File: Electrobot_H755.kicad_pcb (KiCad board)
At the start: 2 copper layers, 32 parts, among them J1 Conn_XT30M, J10 Conn_01x04, J11 Conn_01x04, J12 Conn_01x04, J13 Conn_01x04, J14 Conn_01x04, J2 Conn_01x04, J3 Conn_01x04, J4 Conn_01x04, J5 Conn_01x04, J6 Conn_01x04, J7 Conn_01x04, J8 Conn_01x04, J9 Conn_01x04, U2 TSR_1-2450

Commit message: Routage de la carte + fichiers gerber
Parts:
- added ?: , , F.Cu at (86.4, 165.1)
- added ?: , , F.Cu at (88.9, 160.0)
- added ?: , , F.Cu at (96.5, 157.5)
- added ?: , , F.Cu at (134.6, 157.5)
- added ?: , , F.Cu at (132.1, 165.1)
- added ?: , , F.Cu at (78.7, 165.1)
- added ?: , , F.Cu at (101.6, 160.0)
- added ?: , , F.Cu at (116.8, 167.6)
- added ?: , , F.Cu at (81.3, 157.5)
- added ?: , , F.Cu at (78.7, 167.6)
- added ?: , , F.Cu at (111.8, 167.6)
- added ?: , , F.Cu at (109.2, 162.6)
- added ?: , , F.Cu at (86.4, 167.6)
- added ?: , , F.Cu at (81.3, 167.6)
- added ?: , , F.Cu at (134.6, 162.6)
- added ?: , , F.Cu at (101.6, 167.6)
- added ?: , , F.Cu at (88.9, 157.5)
- added ?: , , F.Cu at (96.5, 167.6)
- added ?: , , F.Cu at (106.7, 157.5)
- added ?: , , F.Cu at (114.3, 162.6)
- added ?: , , F.Cu at (106.7, 160.0)
- added ?: , , F.Cu at (129.5, 162.6)
- added ?: , , F.Cu at (106.7, 167.6)
- added ?: , , F.Cu at (104.1, 165.1)
- added ?: , , F.Cu at (111.8, 165.1)
- added ?: , , F.Cu at (116.8, 165.1)
- added ?: , , F.Cu at (96.5, 160.0)
- added ?: , , F.Cu at (111.8, 162.6)
- added ?: , , F.Cu at (91.4, 157.5)
- added ?: , , F.Cu at (129.5, 160.0)
- added ?: , , F.Cu at (83.8, 162.6)
- added ?: , , F.Cu at (116.8, 157.5)
- added ?: , , F.Cu at (91.4, 165.1)
- added ?: , , F.Cu at (119.4, 160.0)
- added ?: , , F.Cu at (124.5, 160.0)
- added ?: , , F.Cu at (132.1, 167.6)
- added ?: , , F.Cu at (121.9, 167.6)
- added ?: , , F.Cu at (119.4, 167.6)
- added ?: , , F.Cu at (127.0, 165.1)
- added ?: , , F.Cu at (124.5, 162.6)
- added ?: , , F.Cu at (91.4, 162.6)
- added ?: , , F.Cu at (99.1, 160.0)
- added ?: , , F.Cu at (104.1, 162.6)
- added ?: , , F.Cu at (104.1, 157.5)
- added ?: , , F.Cu at (83.8, 160.0)
- added ?: , , F.Cu at (88.9, 165.1)
- added ?: , , F.Cu at (132.1, 157.5)
- added ?: , , F.Cu at (109.2, 167.6)
- added ?: , , F.Cu at (114.3, 160.0)
- added ?: , , F.Cu at (127.0, 157.5)
- added ?: , , F.Cu at (116.8, 160.0)
- added ?: , , F.Cu at (94.0, 160.0)
- added ?: , , F.Cu at (94.0, 165.1)
- added ?: , , F.Cu at (119.4, 157.5)
- added ?: , , F.Cu at (83.8, 165.1)
- added ?: , , F.Cu at (99.1, 157.5)
- added ?: , , F.Cu at (86.4, 162.6)
- added ?: , , F.Cu at (99.1, 167.6)
- added ?: , , F.Cu at (96.5, 162.6)
- added ?: , , F.Cu at (124.5, 165.1)
- added ?: , , F.Cu at (99.1, 162.6)
- added ?: , , F.Cu at (88.9, 162.6)
- added ?: , , F.Cu at (83.8, 167.6)
- added ?: , , F.Cu at (106.7, 162.6)
- added ?: , , F.Cu at (121.9, 157.5)
- added ?: , , F.Cu at (111.8, 160.0)
- added ?: , , F.Cu at (101.6, 165.1)
- added ?: , , F.Cu at (81.3, 160.0)
- added ?: , , F.Cu at (91.4, 167.6)
- added ?: , , F.Cu at (127.0, 160.0)
- added ?: , , F.Cu at (109.2, 160.0)
- added ?: , , F.Cu at (104.1, 160.0)
- added ?: , , F.Cu at (121.9, 160.0)
- added ?: , , F.Cu at (83.8, 157.5)
- added ?: , , F.Cu at (114.3, 157.5)
- added ?: , , F.Cu at (116.8, 162.6)
- added ?: , , F.Cu at (81.3, 165.1)
- added ?: , , F.Cu at (101.6, 162.6)
- added ?: , , F.Cu at (134.6, 167.6)
- added ?: , , F.Cu at (94.0, 157.5)
- added ?: , , F.Cu at (124.5, 157.5)
- added ?: , , F.Cu at (78.7, 160.0)
- added ?: , , F.Cu at (99.1, 165.1)
- added ?: , , F.Cu at (132.1, 162.6)
- added ?: , , F.Cu at (114.3, 165.1)
- added ?: , , F.Cu at (124.5, 167.6)
- added ?: , , F.Cu at (101.6, 157.5)
- added ?: , , F.Cu at (134.6, 160.0)
- added ?: , , F.Cu at (78.7, 157.5)
- added ?: , , F.Cu at (86.4, 160.0)
- added ?: , , F.Cu at (109.2, 157.5)
- added ?: , , F.Cu at (81.3, 162.6)
- added ?: , , F.Cu at (129.5, 165.1)
- added ?: , , F.Cu at (94.0, 167.6)
- added ?: , , F.Cu at (78.7, 162.6)
- added ?: , , F.Cu at (111.8, 157.5)
- added ?: , , F.Cu at (121.9, 162.6)
- added ?: , , F.Cu at (114.3, 167.6)
- added ?: , , F.Cu at (106.7, 165.1)
- added ?: , , F.Cu at (129.5, 167.6)
- added ?: , , F.Cu at (109.2, 165.1)
- added ?: , , F.Cu at (86.4, 157.5)
- added ?: , , F.Cu at (88.9, 167.6)
- added ?: , , F.Cu at (94.0, 162.6)
- added ?: , , F.Cu at (132.1, 160.0)
- added ?: , , F.Cu at (91.4, 160.0)
- added ?: , , F.Cu at (134.6, 165.1)
- added ?: , , F.Cu at (119.4, 165.1)
- added ?: , , F.Cu at (119.4, 162.6)
- added ?: , , F.Cu at (127.0, 162.6)
- added ?: , , F.Cu at (121.9, 165.1)
- added ?: , , F.Cu at (129.5, 157.5)
- added ?: , , F.Cu at (104.1, 167.6)
- added ?: , , F.Cu at (96.5, 165.1)
- added ?: , , F.Cu at (127.0, 167.6)
- added C10: 220u, Passive:C_Radial_D8.0mm_H11.5mm_P3.50mm, B.Cu at (91.9, 63.8)
- added C11: 220u, Passive:C_Radial_D8.0mm_H11.5mm_P3.50mm, B.Cu at (114.5, 53.0)
- added C12: 220u, Passive:C_Radial_D8.0mm_H11.5mm_P3.50mm, B.Cu at (114.5, 41.7)
- added C13: Value, Capacitor_SMD:C_1206_3216Metric, F.Cu at (102.4, 72.1)
- added C14: 100n, Capacitor_SMD:C_1206_3216Metric, F.Cu at (114.6, 122.2)
- added C15: 100n, Capacitor_SMD:C_1206_3216Metric, F.Cu at (148.1, 130.6)
- added C16: 100n, Capacitor_SMD:C_1206_3216Metric, F.Cu at (81.3, 74.9)
- added C17: Value, Capacitor_SMD:C_1206_3216Metric, B.Cu at (136.1, 90.2)
- added C18: 100n, Capacitor_SMD:C_1206_3216Metric, F.Cu at (114.8, 95.5)
- added C19: 100n, Capacitor_SMD:C_1206_3216Metric, F.Cu at (93.7, 85.1)
- added C20: 100n, Capacitor_SMD:C_1206_3216Metric, F.Cu at (96.3, 101.9)
- added C3: Value, Capacitor_SMD:C_1206_3216Metric, F.Cu at (122.2, 132.8)
- added C6: Value, Capacitor_SMD:C_1206_3216Metric, F.Cu at (74.7, 106.7)
- added C7: Value, Capacitor_SMD:C_1206_3216Metric, F.Cu at (69.3, 121.9)
- added C8: Value, Capacitor_SMD:C_1206_3216Metric, F.Cu at (135.9, 84.1)
- added C9: 47u, Capacitor_SMD:C_1206_3216Metric, F.Cu at (119.1, 142.0)
- added D4: LED, LED_SMD:LED_1206_3216Metric, B.Cu at (107.0, 147.8)
- added J15: Conn_01x03, Connector_Molex:Molex_KK-254_AE-6410-03A_1x03_P2.54mm_Vertical, B.Cu at (122.8, 138.7)
- added J16: Conn_01x03, Connector_Molex:Molex_KK-254_AE-6410-03A_1x03_P2.54mm_Vertical, B.Cu at (68.0, 103.6)
- added J17: Conn_01x04, Connector_Molex:Molex_KK-254_AE-6410-04A_1x04_P2.54mm_Vertical, B.Cu at (139.2, 85.2)
- added J18: Conn_01x03, Servomotors:Servomotor-3x254, B.Cu at (129.3, 60.2)
- added J19: Conn_01x03, Servomotors:Servomotor-3x254, B.Cu at (129.3, 50.3)
- added J20: Conn_01x03, Servomotors:Servomotor-3x254, B.Cu at (129.3, 56.9)
- added J21: Conn_01x03, Servomotors:Servomotor-3x254, B.Cu at (129.3, 47.0)
- added J22: Conn_01x04, Connector_Molex:Molex_KK-254_AE-6410-04A_1x04_P2.54mm_Vertical, B.Cu at (145.1, 98.5)
- added J23: Conn_01x03, Servomotors:Servomotor-3x254, B.Cu at (129.3, 43.7)
- added J24: Conn_01x03, Servomotors:Servomotor-3x254, B.Cu at (129.3, 40.3)
- added J25: Conn_01x03, Servomotors:Servomotor-3x254, B.Cu at (129.3, 53.6)
- added J26: Conn_01x03, Connector_Molex:Molex_KK-254_AE-6410-03A_1x03_P2.54mm_Vertical, B.Cu at (68.0, 115.7)
- added J27: Conn_01x02, Connector_Molex:Molex_KK-254_AE-6410-02A_1x02_P2.54mm_Vertical, B.Cu at (77.8, 118.2)
- added J28: Conn_01x02, Connector_Molex:Molex_KK-254_AE-6410-02A_1x02_P2.54mm_Vertical, B.Cu at (77.8, 110.0)
- added J29: Conn_01x02, Connector_Molex:Molex_KK-254_AE-6410-02A_1x02_P2.54mm_Vertical, B.Cu at (139.4, 66.7)
- added J30: Conn_01x02, Connector_Molex:Molex_KK-254_AE-6410-02A_1x02_P2.54mm_Vertical, B.Cu at (139.4, 75.0)
- added J31: Conn_01x03, Connector_Molex:Molex_KK-254_AE-6410-03A_1x03_P2.54mm_Vertical, B.Cu at (92.4, 99.1)
- added J32: Conn_01x03, Connector_Molex:Molex_KK-254_AE-6410-03A_1x03_P2.54mm_Vertical, B.Cu at (77.1, 95.8)
- added J33: Conn_01x06, Connector_Molex:Molex_KK-254_AE-6410-06A_1x06_P2.54mm_Vertical, B.Cu at (92.4, 79.5)
- added J34: Conn_01x06, Connector_Molex:Molex_KK-254_AE-6410-06A_1x06_P2.54mm_Vertical, B.Cu at (92.4, 90.3)
- added J35: Conn_01x04, Connector_Molex:Molex_KK-254_AE-6410-04A_1x04_P2.54mm_Vertical, B.Cu at (139.9, 134.1)
- added J36: Conn_01x02, Connector_Molex:Molex_KK-254_AE-6410-02A_1x02_P2.54mm_Vertical, B.Cu at (77.1, 87.1)
- added J37: Conn_01x04, Connector_Molex:Molex_KK-254_AE-6410-04A_1x04_P2.54mm_Vertical, B.Cu at (139.7, 109.2)
- added JP1: SolderJumper_2_Open, Connector_PinHeader_2.54mm:PinHeader_1x02_P2.54mm_Vertical, B.Cu at (122.8, 47.9)
- added R1: 10k, Resistor_SMD:R_1206_3216Metric, F.Cu at (120.1, 103.8)
- added R10: 10k, Resistor_SMD:R_1206_3216Metric, F.Cu at (122.7, 121.9)
- added R11: 10k, Resistor_SMD:R_1206_3216Metric, F.Cu at (122.4, 77.0)
- added R12: 10k, Resistor_SMD:R_1206_3216Metric, F.Cu at (125.0, 69.3)
- added R13: 18k, Resistor_SMD:R_1206_3216Metric, F.Cu at (122.7, 119.1)
- added R14: 18k, Resistor_SMD:R_1206_3216Metric, F.Cu at (124.5, 126.0)
- added R15: 18k, Resistor_SMD:R_1206_3216Metric, F.Cu at (125.2, 82.0)
- added R16: 18k, Resistor_SMD:R_1206_3216Metric, F.Cu at (125.0, 66.3)
- added R2: 18k, Resistor_SMD:R_1206_3216Metric, F.Cu at (135.9, 101.6)
- added R22: R, Resistor_SMD:R_1206_3216Metric, B.Cu at (126.2, 137.2)
- added R23: R, Resistor_SMD:R_1206_3216Metric, F.Cu at (122.2, 135.4)
- added R24: R, Resistor_SMD:R_1206_3216Metric, B.Cu at (69.3, 106.7)
- added R25: R, Resistor_SMD:R_1206_3216Metric, F.Cu at (70.9, 102.6)
- added R26: R, Resistor_SMD:R_1206_3216Metric, B.Cu at (69.3, 118.6)
- added R27: R, Resistor_SMD:R_1206_3216Metric, F.Cu at (72.4, 115.6)
- added R28: R, Resistor_SMD:R_1206_3216Metric, B.Cu at (136.9, 80.2)
- added R29: R, Resistor_SMD:R_1206_3216Metric, B.Cu at (135.4, 84.1)
- added R3: 10k, Resistor_SMD:R_1206_3216Metric, F.Cu at (120.4, 97.5)
- added R30: 39k, Resistor_SMD:R_1206_3216Metric, F.Cu at (102.4, 69.1)
- added R31: 10k, Resistor_SMD:R_1206_3216Metric, F.Cu at (80.0, 104.6)
- added R32: 10k, Resistor_SMD:R_1206_3216Metric, F.Cu at (92.7, 110.5)
- added R33: 18k, Resistor_SMD:R_1206_3216Metric, F.Cu at (89.9, 113.3)
- added R34: 10k, Resistor_SMD:R_1206_3216Metric, F.Cu at (136.1, 95.2)
- added R35: 18k, Resistor_SMD:R_1206_3216Metric, F.Cu at (136.1, 92.2)
- added R36: 470, Resistor_SMD:R_1206_3216Metric, F.Cu at (106.9, 149.1)
- added R37: R, Resistor_SMD:R_1206_3216Metric, B.Cu at (142.0, 89.9)
- added R38: R, Resistor_SMD:R_1206_3216Metric, F.Cu at (136.1, 89.7)
- added R4: 18k, Resistor_SMD:R_1206_3216Metric, F.Cu at (79.8, 121.7)
- added R5: 10k, Resistor_SMD:R_1206_3216Metric, F.Cu at (120.1, 88.3)
- added R6: 10k, Resistor_SMD:R_1206_3216Metric, F.Cu at (125.2, 91.9)
- added R7: 18k, Resistor_SMD:R_1206_3216Metric, F.Cu at (125.2, 84.8)
- added R8: 18k, Resistor_SMD:R_1206_3216Metric, F.Cu at (125.2, 94.7)
- added R9: 10k, Resistor_SMD:R_1206_3216Metric, F.Cu at (119.9, 129.5)
- added U3: TSR_2-2465, Converter_DCDC:Converter_DCDC_TRACO_TSR-1_THT, B.Cu at (99.2, 52.5)
- added U4: TSR_2-2465, Converter_DCDC:Converter_DCDC_TRACO_TSR-1_THT, B.Cu at (99.2, 41.7)
- C4: footprint Capacitor_THT:C_Radial_D8.0mm_H11.5mm_P3.50mm -> Passive:C_Radial_D8.0mm_H11.5mm_P3.50mm; moved to B.Cu
- D1, D2, D3, J1: moved to B.Cu
- U2: value TSR_1-2450 -> TSR_2-2450; moved to B.Cu
- moved H3 170.4 mm to (147.3, 40.7)
- moved H4 117.0 mm to (147.3, 166.4)
- moved H1 114.5 mm to (68.2, 40.7)
- moved U2 107.3 mm to (88.4, 56.1), turned to 180 degrees
- moved C1 100.2 mm to (84.8, 52.8)
- moved J5 96.9 mm to (77.1, 134.7), turned to 90 degrees
- moved J2 93.5 mm to (92.3, 126.2), turned to 90 degrees
- moved J3 92.6 mm to (92.4, 132.8), turned to -90 degrees
- moved C2 89.9 mm to (74.2, 97.0), turned to -90 degrees
- moved J6 88.3 mm to (97.5, 108.0), turned to -90 degrees
- moved J1 75.0 mm to (84.0, 42.2)
- moved J9 71.4 mm to (113.5, 125.5), turned to 0 degrees
- moved R17 68.1 mm to (141.6, 157.3), turned to 90 degrees
- moved J7 66.8 mm to (113.5, 100.7), turned to 0 degrees
- moved R18 64.1 mm to (144.7, 157.3), turned to 90 degrees
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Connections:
- J6 pad 1: /RS232_1_TX -> /RS232_2_TX
- J6 pad 2: /RS232_1_RX -> Net-(J6-Pin_2)
- J6 pad 3: /RS232_1_GPIO -> /RS232_2_DIR
- R19 pad 1: /LED1 -> /LED4
- R20 pad 1: /LED2 -> /LED5
- R21 pad 1: /LED3 -> /LED6
- U1 pad CN10_10: unconnected-(U1-PE13-PadCN10_10) -> /Mot3_Sens2
- U1 pad CN10_12: unconnected-(U1-PG14-PadCN10_12) -> /RS232_3_TX
- U1 pad CN10_14: unconnected-(U1-PB6-PadCN10_14) -> /I2C_SCL
- U1 pad CN10_15: unconnected-(U1-PB2-PadCN10_15) -> /SPI_MOSI
- U1 pad CN10_16: unconnected-(U1-PB7-PadCN10_16) -> /I2C_SDA
- U1 pad CN10_17: unconnected-(U1-GND-PadCN10_17) -> GND
- U1 pad CN10_18: unconnected-(U1-PE8-PadCN10_18) -> /LED5
- U1 pad CN10_19: unconnected-(U1-PD13-PadCN10_19) -> /CODER_3_B
- U1 pad CN10_20: unconnected-(U1-PE7-PadCN10_20) -> /LED4
- U1 pad CN10_21: unconnected-(U1-PD12-PadCN10_21) -> /CODER_3_A
- U1 pad CN10_22: unconnected-(U1-GND-PadCN10_22) -> GND
- U1 pad CN10_23: unconnected-(U1-PD11-PadCN10_23) -> /Mot2_Sens2
- U1 pad CN10_26: unconnected-(U1-PE12-PadCN10_26) -> /LED6
- U1 pad CN10_27: unconnected-(U1-GND-PadCN10_27) -> GND
- U1 pad CN10_29: unconnected-(U1-PA0-PadCN10_29) -> /Eana1f
- U1 pad CN10_3: unconnected-(U1-AGND-PadCN10_3) -> GND
- U1 pad CN10_30: unconnected-(U1-PE15-PadCN10_30) -> /LED7
- U1 pad CN10_32: unconnected-(U1-PB10-PadCN10_32) -> /Servo5_PWM
- U1 pad CN10_34: unconnected-(U1-PB11-PadCN10_34) -> /Servo4_PWM
- U1 pad CN10_5: unconnected-(U1-GND-PadCN10_5) -> GND
- U1 pad CN10_6: unconnected-(U1-PE11-PadCN10_6) -> /CODER_1_B
- U1 pad CN10_7: unconnected-(U1-PF6-PadCN10_7) -> /Mot3_PWM
- U1 pad CN10_8: unconnected-(U1-PE14-PadCN10_8) -> /Mot3_Sens1
- U1 pad CN7_1: unconnected-(U1-PC6-PadCN7_1) -> /CODER_4_A
- U1 pad CN7_10: unconnected-(U1-PA5-PadCN7_10) -> /Servo3_PWM
- U1 pad CN7_11: unconnected-(U1-PC7-PadCN7_11) -> /CODER_4_B
- U1 pad CN7_12: unconnected-(U1-PA6-PadCN7_12) -> /Eana4f
- U1 pad CN7_13: unconnected-(U1-PB5-PadCN7_13) -> /CODER_2_B
- U1 pad CN7_15: unconnected-(U1-PB3-PadCN7_15) -> /Servo2_PWM
- U1 pad CN7_17: unconnected-(U1-PA4-PadCN7_17) -> /Eana5f
- U1 pad CN7_19: unconnected-(U1-PB4-PadCN7_19) -> /CODER_2_A
- U1 pad CN7_2: unconnected-(U1-PB8-PadCN7_2) -> /Etor3
- U1 pad CN7_20: unconnected-(U1-PG9-PadCN7_20) -> /RS232_3_RX
- U1 pad CN7_3: unconnected-(U1-PB15-PadCN7_3) -> /Servo1_PWM
- U1 pad CN7_4: unconnected-(U1-PB9-PadCN7_4) -> /Etor4
- U1 pad CN7_8: unconnected-(U1-GND-PadCN7_8) -> GND
- U1 pad CN8_10: unconnected-(U1-PC12-PadCN8_10) -> /LED_RGB
- U1 pad CN8_2: unconnected-(U1-PC8-PadCN8_2) -> /SPI_CS1
- U1 pad CN8_4: unconnected-(U1-PC9-PadCN8_4) -> /SPI_CS2
- U1 pad CN8_5: unconnected-(U1-~{RESET}-PadCN8_5) -> Net-(J36-Pin_1)
- U1 pad CN8_6: unconnected-(U1-PC10-PadCN8_6) -> /SPI_CLK
- U1 pad CN8_8: unconnected-(U1-PC11-PadCN8_8) -> /SPI_MISO
- U1 pad CN9_1: unconnected-(U1-PA3-PadCN9_1) -> /Eana2f
- U1 pad CN9_12: unconnected-(U1-GND-PadCN9_12) -> GND
- U1 pad CN9_14: unconnected-(U1-PE2-PadCN9_14) -> /Mot1_Sens1
- U1 pad CN9_15: unconnected-(U1-PE9-PadCN9_15) -> /CODER_1_A
- U1 pad CN9_16: unconnected-(U1-PE4-PadCN9_16) -> /Mot1_Sens2
- U1 pad CN9_18: unconnected-(U1-PE5-PadCN9_18) -> /Mot1_PWM
- U1 pad CN9_19: unconnected-(U1-PF14-PadCN9_19) -> /Mot4_Sens1
- U1 pad CN9_20: unconnected-(U1-PE6-PadCN9_20) -> /Mot2_PWM
- U1 pad CN9_21: unconnected-(U1-PF15-PadCN9_21) -> /Mot4_Sens2
- U1 pad CN9_22: unconnected-(U1-PE3-PadCN9_22) -> /Mot2_Sens1
- U1 pad CN9_23: unconnected-(U1-GND-PadCN9_23) -> GND
- U1 pad CN9_24: unconnected-(U1-PF8-PadCN9_24) -> /Servo6_PWM
- U1 pad CN9_26: unconnected-(U1-PF7-PadCN9_26) -> /Mot4_PWM
- U1 pad CN9_28: unconnected-(U1-PF9-PadCN9_28) -> /Servo7_PWM
- U1 pad CN9_3: unconnected-(U1-PC0-PadCN9_3) -> /VBATf
- U1 pad CN9_4: unconnected-(U1-PD6-PadCN9_4) -> /RS232_2_RX
- U1 pad CN9_5: unconnected-(U1-PC3-PadCN9_5) -> /Etor2
- U1 pad CN9_6: unconnected-(U1-PD5-PadCN9_6) -> /RS232_2_TX
- U1 pad CN9_7: unconnected-(U1-PB1-PadCN9_7) -> /Eana3f
- U1 pad CN9_8: unconnected-(U1-PD4-PadCN9_8) -> /RS232_2_DIR
- U1 pad CN9_9: unconnected-(U1-PC2-PadCN9_9) -> /Etor1
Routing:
- net +5V: track 0.00 -> 494.7 mm, vias 0 -> 1
- net GND: track 0.00 -> 281.7 mm, vias 0 -> 1
- net /Servo7_PWM: track 0.00 -> 161.3 mm
- net +3.3V: track 0.00 -> 159.1 mm, vias 0 -> 1
- net /Servo5_PWM: track 0.00 -> 124.5 mm
- net /Servo6_PWM: track 0.00 -> 116.9 mm
- net /I2C_SCL: track 0.00 -> 101.4 mm
- net /Servo4_PWM: track 0.00 -> 100.6 mm
- net /I2C_SDA: track 0.00 -> 83.3 mm
- net /SPI_MOSI: track 0.00 -> 60.5 mm, vias 0 -> 1
- net /CODER_1_A: track 0.00 -> 58.9 mm, vias 0 -> 1
- net /VBATf: track 0.00 -> 58.0 mm, vias 0 -> 1
- net /LED5: track 0.00 -> 56.0 mm
- net /VBAT: track 0.00 -> 54.3 mm
- net /+Vservo1: track 0.00 -> 51.0 mm
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- added copper zone on B.Cu, net GND
- added copper zone on F.Cu, net GND
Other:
- board outline added: 88.3 x 136 mm
- board text added: "+"
- board text added: "+3.3V"
- board text added: "+5V"
- board text added: "-"
- board text added: "1"
- board text added: "2"
- board text added: "3"
- board text added: "4"
- board text added: "5"
- board text added: "6"
- board text added: "7"
- board text added: "CS1"
- board text added: "CS2"
- board text added: "Codeur1"
- board text added: "Codeur2"
- board text added: "Codeur3"
- board text added: "Codeur4"
- board text added: "Dir"
- board text added: "ELECTROBOT_H755 V1 (2025)"
- board text added: "Eana"
- board text added: "Etor"
- board text added: "GND"
- board text added: "I2C"
- board text added: "I2C_SCL"
- board text added: "I2C_SDA"
- board text added: "MISO"
- board text added: "MOSI"
- board text added: "Moteur1"
- board text added: "Moteur2"
- board text added: "Moteur3"
- board text added: "Moteur4"
- board text added: "PROTOTYPAGE"
- board text added: "RS232"
- board text added: "RS232 AX"
- board text added: "RX"
- board text added: "Reset"
- board text added: "SCK"
- board text added: "SCL"
- board text added: "SDA"
- board text added: "SPI"
- board text added: "Servo"
- board text added: "TX"

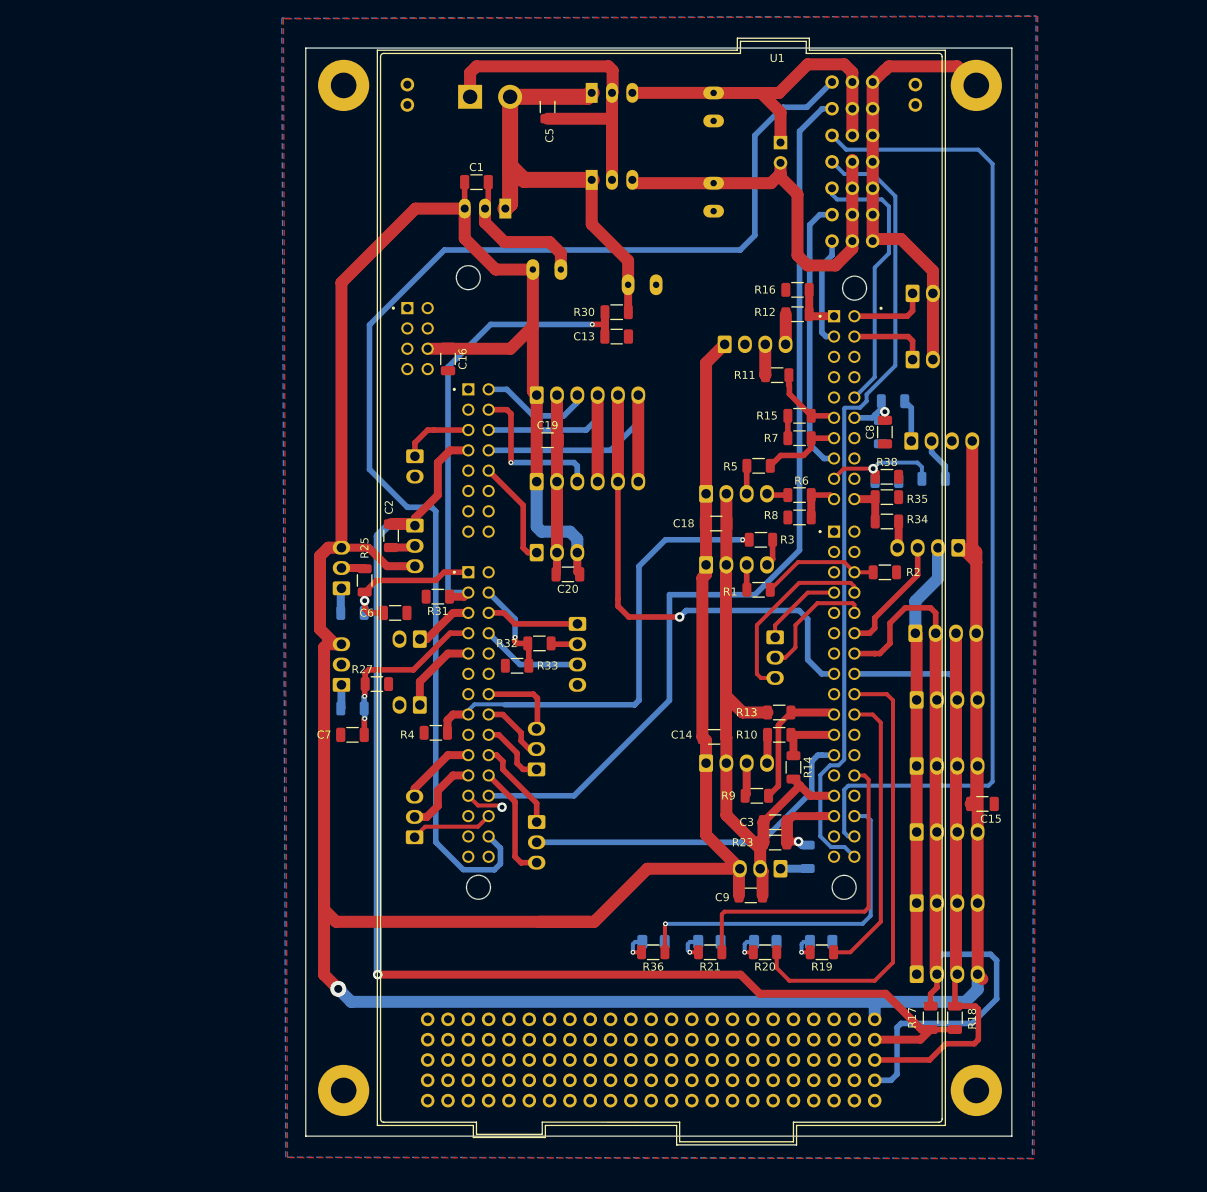
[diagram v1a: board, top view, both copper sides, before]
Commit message: Bords de la carte arrondis + ajout sérigraphie manquante
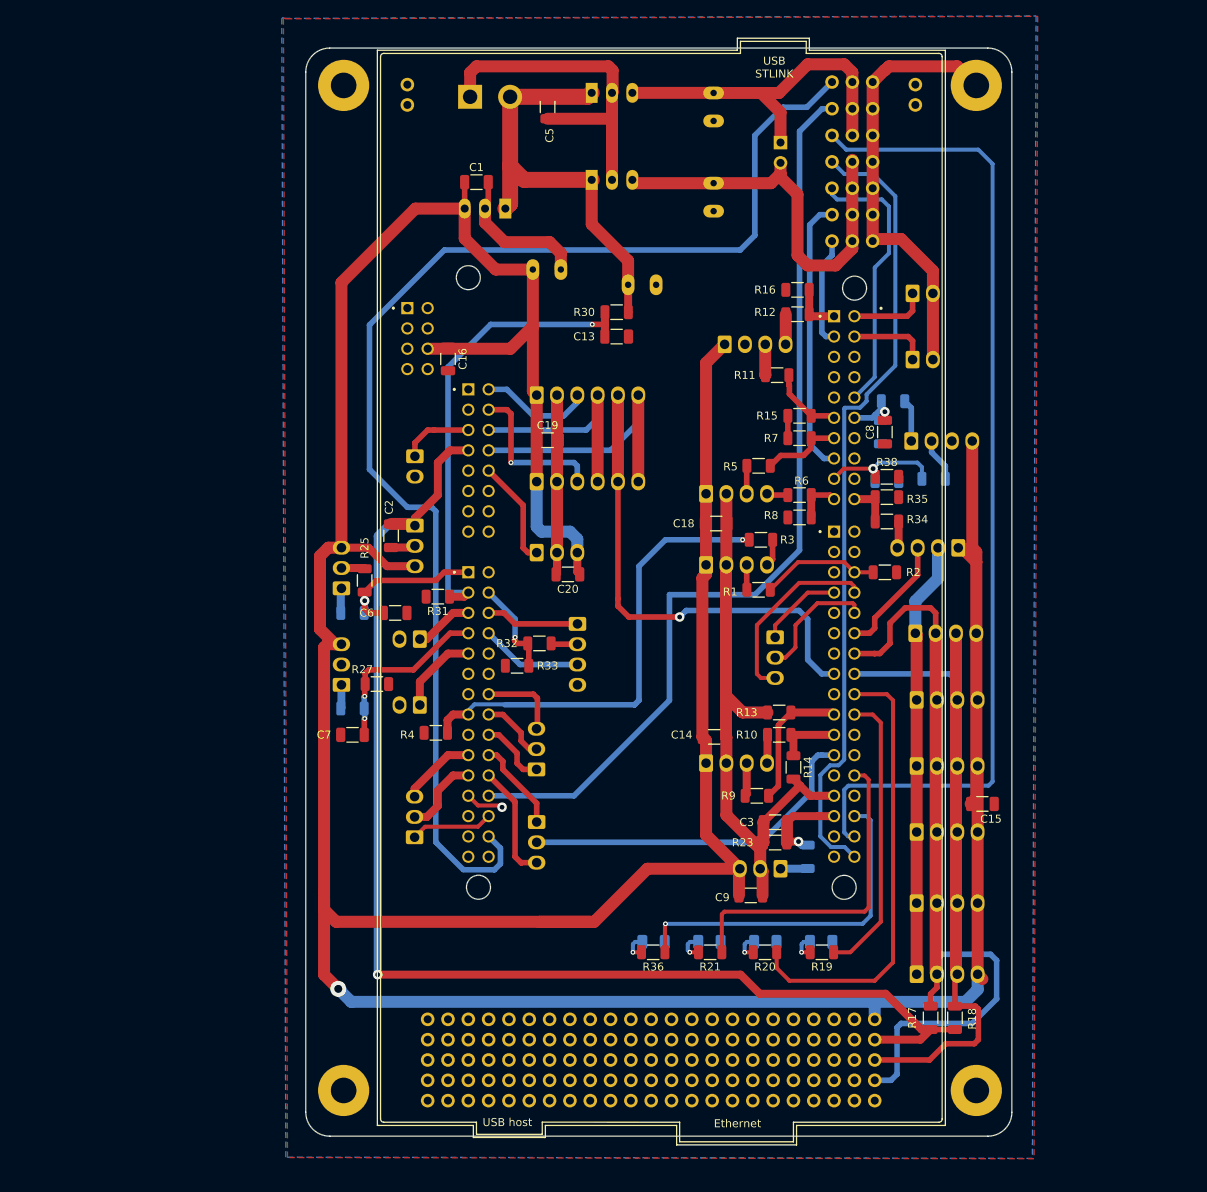
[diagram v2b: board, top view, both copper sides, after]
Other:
- outline, holes or cut-outs redrawn
- board text added: "Ethernet"
- board text added: "USB STLINK"
- board text added: "USB host"
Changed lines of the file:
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@@
 			(at 46.228 -31.242 0)
 			(layer "F.SilkS")
+			(hide yes)
 			(effects
 				(font
@@
 		(layer "B.SilkS")
 	)
-	(gr_rect
-		(start 63.5 36.068)
-		(end 151.765 172.085)
+	(gr_arc
+		(start 66.5 172.085)
+		(mid 64.37868 171.20632)
+		(end 63.5 169.085)
+		(locked yes)
+		(stroke
+			(width 0.05)
+			(type default)
+		)
+		(layer "Edge.Cuts")
+	)
+	(gr_line
+		(start 148.765 172.085)
+		(end 66.5 172.085)
+		(locked yes)
+		(stroke
+			(width 0.05)
+			(type default)
+		)
+		(layer "Edge.Cuts")
+	)
+	(gr_line
+		(start 66.5 36.068)
+		(end 148.765 36.068)
+		(locked yes)
+		(stroke
+			(width 0.05)
+			(type default)
+		)
+		(layer "Edge.Cuts")
+	)
+	(gr_line
+		(start 151.765 39.068)
+		(end 151.765 169.085)
+		(locked yes)
+		(stroke
+			(width 0.05)
+			(type default)
+		)
+		(layer "Edge.Cuts")
+	)
+	(gr_arc
+		(start 148.765 36.068)
+		(mid 150.88632 36.94668)
+		(end 151.765 39.068)
+		(locked yes)
+		(stroke
+			(width 0.05)
+			(type default)
+		)
+		(layer "Edge.Cuts")
+	)
+	(gr_arc
+		(start 151.765 169.085)
+		(mid 150.88632 171.20632)
+		(end 148.765 172.085)
+		(locked yes)
+		(stroke
+			(width 0.05)
+			(type default)
+		)
+		(layer "Edge.Cuts")
+	)
+	(gr_line
+		(start 63.5 169.085)
+		(end 63.5 39.068)
+		(locked yes)
+		(stroke
+			(width 0.05)
+			(type default)
+		)
+		(layer "Edge.Cuts")
+	)
+	(gr_arc
+		(start 63.5 39.068)
+		(mid 64.37868 36.94668)
+		(end 66.5 36.068)
 		(locked yes)
 		(stroke
@@
 			(type default)
 		)
-		(fill none)
 		(layer "Edge.Cuts")
 	)
@@
 		)
 	)
+	(gr_text "USB host"
+		(at 85.598 170.942 -0)
+		(layer "F.SilkS")
+		(effects
+			(font
+				(size 1 1)
+				(thickness 0.1)
+			)
+			(justify left bottom)
+		)
+	)
+	(gr_text "Ethernet"
+		(at 114.5032 171.0944 -0)
+		(layer "F.SilkS")
+		(effects
+			(font
+				(size 1 1)
+				(thickness 0.1)
+			)
+			(justify left bottom)
+		)
+	)
+	(gr_text "USB\nSTLINK"
+		(at 122.0724 39.878 0)
+		(layer "F.SilkS")
+		(effects
+			(font
+				(size 1 1)
+				(thickness 0.1)
+			)
+			(justify bottom)
+		)
+	)

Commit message: Ajout sérigraphie manquante
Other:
- board text added: "A"
- board text added: "K"
- board text added: "PWM"
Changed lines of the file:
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@@
+		)
+	)
+	(gr_text "A"
+		(at 126.8984 150.368 0)
+		(layer "B.SilkS")
+		(effects
+			(font
+				(size 1 1)
+				(thickness 0.1)
+			)
+			(justify left bottom mirror)
 		)
 	)
@@
 		)
 	)
+	(gr_text "A"
+		(at 113.0808 150.3172 0)
+		(layer "B.SilkS")
+		(effects
+			(font
+				(size 1 1)
+				(thickness 0.1)
+			)
+			(justify left bottom mirror)
+		)
+	)
+	(gr_text "+"
+		(at 132.2832 62.0268 90)
+		(layer "B.SilkS")
+		(effects
+			(font
+				(size 1 1)
+				(thickness 0.1)
+			)
+			(justify left bottom mirror)
+		)
+	)
 	(gr_text "1"
 		(at 127.5588 60.8584 0)
@@
 		)
 	)
+	(gr_text "A"
+		(at 119.9896 150.368 0)
+		(layer "B.SilkS")
+		(effects
+			(font
+				(size 1 1)
+				(thickness 0.1)
+			)
+			(justify left bottom mirror)
+		)
+	)
 	(gr_text "-"
 		(at 143.002 93.472 90)
@@
 		)
 	)
+	(gr_text "-"
+		(at 95.9612 60.9092 90)
+		(layer "B.SilkS")
+		(effects
+			(font
+				(size 1 1)
+				(thickness 0.1)
+			)
+			(justify left bottom mirror)
+		)
+	)
+	(gr_text "-"
+		(at 116.1796 44.6532 180)
+		(layer "B.SilkS")
+		(effects
+			(font
+				(size 1 1)
+				(thickness 0.1)
+			)
+			(justify left bottom mirror)
+		)
+	)
 	(gr_text "+5V"
 		(at 136.398 156.4132 0)
@@
 		)
 	)
+	(gr_text "K"
+		(at 116.078 150.368 0)
+		(layer "B.SilkS")
+		(effects
+			(font
+				(size 1 1)
+				(thickness 0.1)
+			)
+			(justify left bottom mirror)
+		)
+	)
 	(gr_text "5"
 		(at 127.5588 47.6504 0)
@@
 		)
 	)
+	(gr_text "-"
+		(at 134.9248 62.1792 90)
+		(layer "B.SilkS")
+		(effects
+			(font
+				(size 1 1)
+				(thickness 0.1)
+			)
+			(justify left bottom mirror)
+		)
+	)
 	(gr_text "+"
 		(at 114.1984 87.1728 90)
@@
 		)
 	)
+	(gr_text "+"
+		(at 117.1448 40.9448 90)
+		(layer "B.SilkS")
+		(effects
+			(font
+				(size 1 1)
+				(thickness 0.1)
+			)
+			(justify left bottom mirror)
+		)
+	)
 	(gr_text "-"
 		(at 95.5548 84.4804 90)
@@
 		)
 	)
+	(gr_text "PWM"
+		(at 129.6924 62.23 90)
+		(layer "B.SilkS")
+		(effects
+			(font
+				(size 1 1)
+				(thickness 0.1)
+				(italic yes)
+			)
+			(justify left bottom mirror)
+		)
+	)
+	(gr_text "K"
+		(at 129.8448 150.4188 0)
+		(layer "B.SilkS")
+		(effects
+			(font
+				(size 1 1)
+				(thickness 0.1)
+			)
+			(justify left bottom mirror)
+		)
+	)
 	(gr_text "-"
 		(at 101.346 115.316 180)
@@
 		)
 	)
+	(gr_text "+"
+		(at 104.2924 62.4332 90)
+		(layer "B.SilkS")
+		(effects
+			(font
+				(size 1 1)
+				(thickness 0.1)
+			)
+			(justify left bottom mirror)
+		)
+	)
 	(gr_text "Codeur2"
 		(at 111.2012 88.5444 90)
@@
 	)
 	(gr_text "-"
+		(at 107.8992 62.3824 90)
+		(layer "B.SilkS")
+		(effects
+			(font
+				(size 1 1)
+				(thickness 0.1)
+			)
+			(justify left bottom mirror)
+		)
+	)
+	(gr_text "K"
+		(at 108.9152 150.4696 0)
+		(layer "B.SilkS")
+		(effects
+			(font
+				(size 1 1)
+				(thickness 0.1)
+			)
+			(justify left bottom mirror)
+		)
+	)
+	(gr_text "-"
 		(at 116.6368 104.2924 90)
 		(layer "B.SilkS")
@@
 		)
 	)
+	(gr_text "K"
+		(at 122.8852 150.4188 0)
+		(layer "B.SilkS")
+		(effects
+			(font
+				(size 1 1)
+				(thickness 0.1)
+			)
+			(justify left bottom mirror)
+		)
+	)
 	(gr_text "+"
 		(at 116.5352 68.4784 90)
@@
 	)
 	(gr_text "-"
+		(at 116.1288 55.9308 180)
+		(layer "B.SilkS")
+		(effects
+			(font
+				(size 1 1)
+				(thickness 0.1)
+			)
+			(justify left bottom mirror)
+		)
+	)
+	(gr_text "-"
 		(at 145.034 80.518 90)
 		(layer "B.SilkS")
@@
 		)
 	)
+	(gr_text "+"
+		(at 92.456 60.8076 90)
+		(layer "B.SilkS")
+		(effects
+			(font
+				(size 1 1)
+				(thickness 0.1)
+			)
+			(justify left bottom mirror)
+		)
+	)
 	(gr_text "-"
 		(at 81.026 97.79 180)
@@
 		)
 	)
+	(gr_text "A"
+		(at 106.0704 150.4696 0)
+		(layer "B.SilkS")
+		(effects
+			(font
+				(size 1 1)
+				(thickness 0.1)
+			)
+			(justify left bottom mirror)
+		)
+	)
 	(gr_text "Moteur3"
 		(at 118.2624 109.4232 90)
@@
 			)
 			(justify left bottom mirror)
+		)
+	)
+	(gr_text "+"
+		(at 117.1956 52.1208 90)
+		(layer "B.SilkS")
+		(effects
+			(font
+				(size 1 1)
+				(thickness 0.1)
+			)
+			(justify left bottom mirror)
